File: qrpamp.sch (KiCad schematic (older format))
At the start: 0 parts

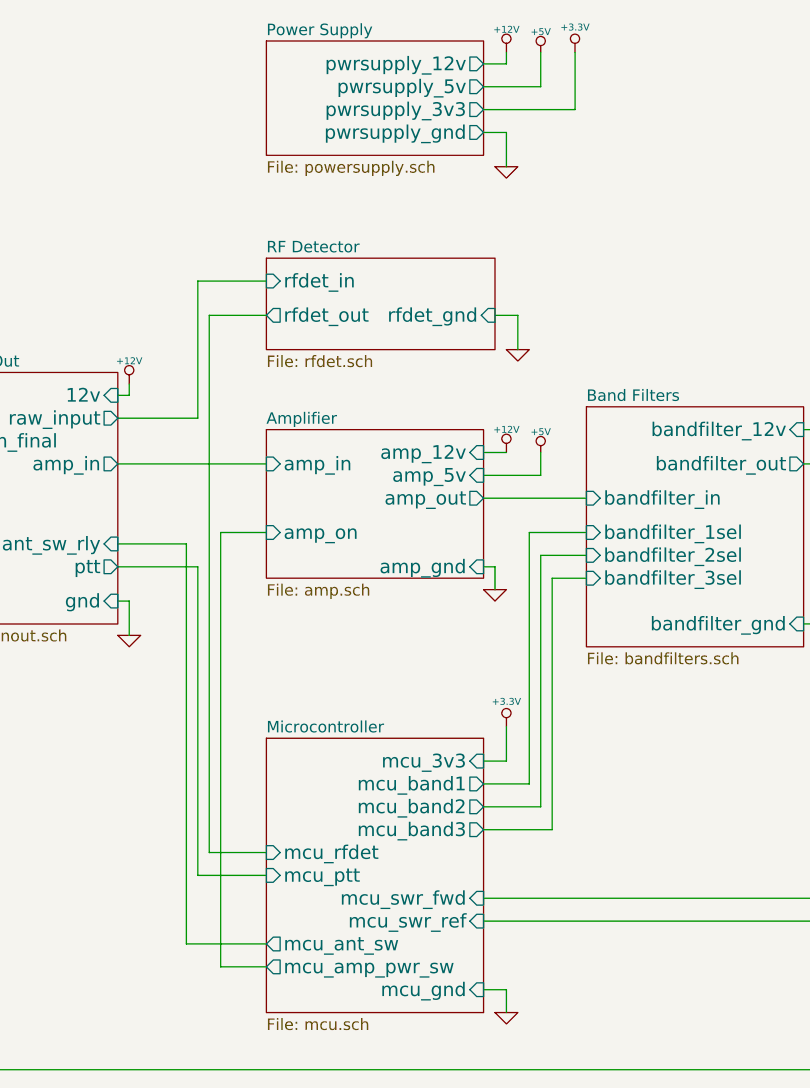
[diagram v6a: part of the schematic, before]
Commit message: Separate analog/digital gnd. Add some filtering caps and reset button.
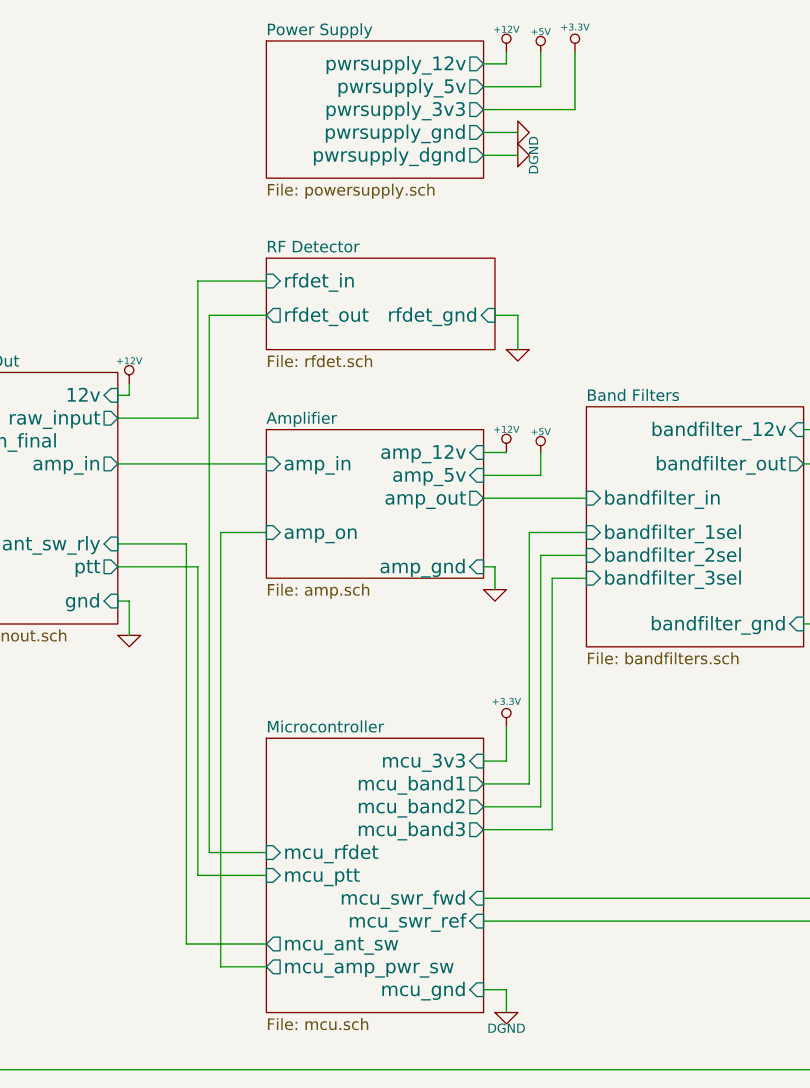
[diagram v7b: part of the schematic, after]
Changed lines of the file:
@@
 $EndSheet
 $Sheet
-S 3250 2000 950  500
+S 3250 2000 950  600
 U 5470C5E9
 F0 "Power Supply" 50
@@
 F4 "pwrsupply_3v3" O R 4200 2300 60
 F5 "pwrsupply_gnd" O R 4200 2400 60
+F6 "pwrsupply_dgnd" O R 4200 2500 60
 $EndSheet
 $Sheet
@@
 L GND #PWR01
 U 1 1 547173E7
-P 4300 2550
-F 0 "#PWR01" H 4300 2550 30  0001 C CNN
-F 1 "GND" H 4300 2480 30  0001 C CNN
-F 2 "" H 4300 2550 60  0000 C CNN
-F 3 "" H 4300 2550 60  0000 C CNN
-	1    4300 2550
-	1    0    0    -1
+P 4350 2400
+F 0 "#PWR01" H 4350 2400 30  0001 C CNN
+F 1 "GND" H 4350 2330 30  0001 C CNN
+F 2 "" H 4350 2400 60  0000 C CNN
+F 3 "" H 4350 2400 60  0000 C CNN
+	1    4350 2400
+	0    -1   -1   0
 $EndComp
 $Comp
@@
 Wire Wire Line
 	4600 2300 4200 2300
-Wire Wire Line
-	4200 2400 4300 2400
-Wire Wire Line
-	4300 2400 4300 2550
 $Comp
 L +12V #PWR05
@@
 Wire Wire Line
 	4300 5150 4300 5000
-$Comp
-L GND #PWR012
-U 1 1 5472B833
-P 4300 6250
-F 0 "#PWR012" H 4300 6250 30  0001 C CNN
-F 1 "GND" H 4300 6180 30  0001 C CNN
-F 2 "" H 4300 6250 60  0000 C CNN
-F 3 "" H 4300 6250 60  0000 C CNN
-	1    4300 6250
-	1    0    0    -1
-$EndComp
 Wire Wire Line
 	4200 6150 4300 6150
@@
 	3050 4150 3250 4150
 $Comp
-L +12V #PWR013
+L +12V #PWR012
 U 1 1 54742ADC
 P 2650 3500
-F 0 "#PWR013" H 2650 3450 20  0001 C CNN
+F 0 "#PWR012" H 2650 3450 20  0001 C CNN
 F 1 "+12V" H 2650 3600 30  0000 C CNN
 F 2 "" H 2650 3500 60  0000 C CNN
@@
 $EndComp
 $Comp
-L GND #PWR014
+L GND #PWR013
 U 1 1 54742BE9
 P 2650 4600
-F 0 "#PWR014" H 2650 4600 30  0001 C CNN
+F 0 "#PWR013" H 2650 4600 30  0001 C CNN
 F 1 "GND" H 2650 4530 30  0001 C CNN
 F 2 "" H 2650 4600 60  0000 C CNN
@@
 	2650 4450 2650 4600
 $Comp
-L GND #PWR015
+L GND #PWR014
 U 1 1 5474324F
 P 4350 3350
-F 0 "#PWR015" H 4350 3350 30  0001 C CNN
+F 0 "#PWR014" H 4350 3350 30  0001 C CNN
 F 1 "GND" H 4350 3280 30  0001 C CNN
 F 2 "" H 4350 3350 60  0000 C CNN
@@
 Wire Wire Line
 	4350 3200 4350 3350
+Wire Wire Line
+	4200 2400 4350 2400
+$Comp
+L DGND #PWR015
+U 1 1 548478BE
+P 4350 2500
+F 0 "#PWR015" H 4350 2500 40  0001 C CNN
+F 1 "DGND" H 4350 2430 40  0000 C CNN
+F 2 "" H 4350 2500 60  0000 C CNN
+F 3 "" H 4350 2500 60  0000 C CNN
+	1    4350 2500
+	0    -1   -1   0
+$EndComp
+Wire Wire Line
+	4200 2500 4350 2500
+$Comp
+L DGND #PWR016
+U 1 1 5484F0B9
+P 4300 6250
+F 0 "#PWR016" H 4300 6250 40  0001 C CNN
+F 1 "DGND" H 4300 6180 40  0000 C CNN
+F 2 "" H 4300 6250 60  0000 C CNN
+F 3 "" H 4300 6250 60  0000 C CNN
+	1    4300 6250
+	1    0    0    -1
+$EndComp
 $EndSCHEMATC

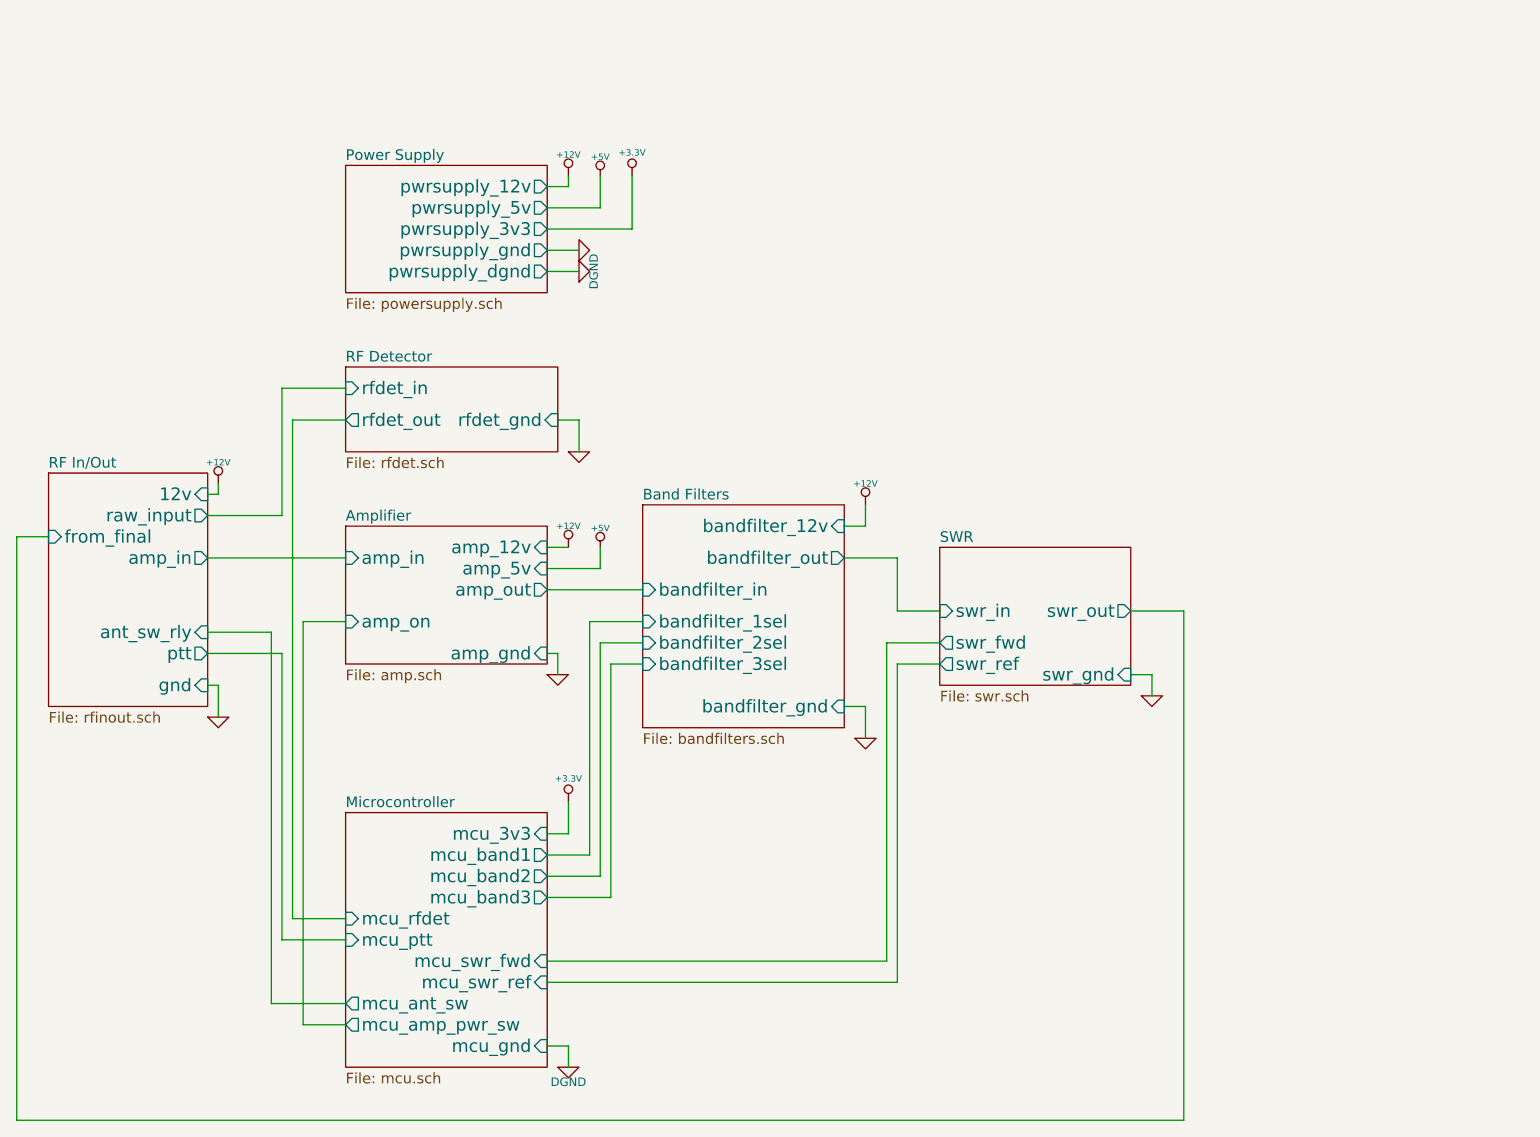
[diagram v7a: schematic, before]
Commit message: Fixed issues found with test board
- Added MOSFETs to relay switch lines from MCU
- Reconnected SWR in/out to actual ADC pins
- Changed LM3940 footprint to SOT223
- Added 4th mounting hole
- Swapped joystick for nav button
- Extended pads of STM32F401 for easier soldering
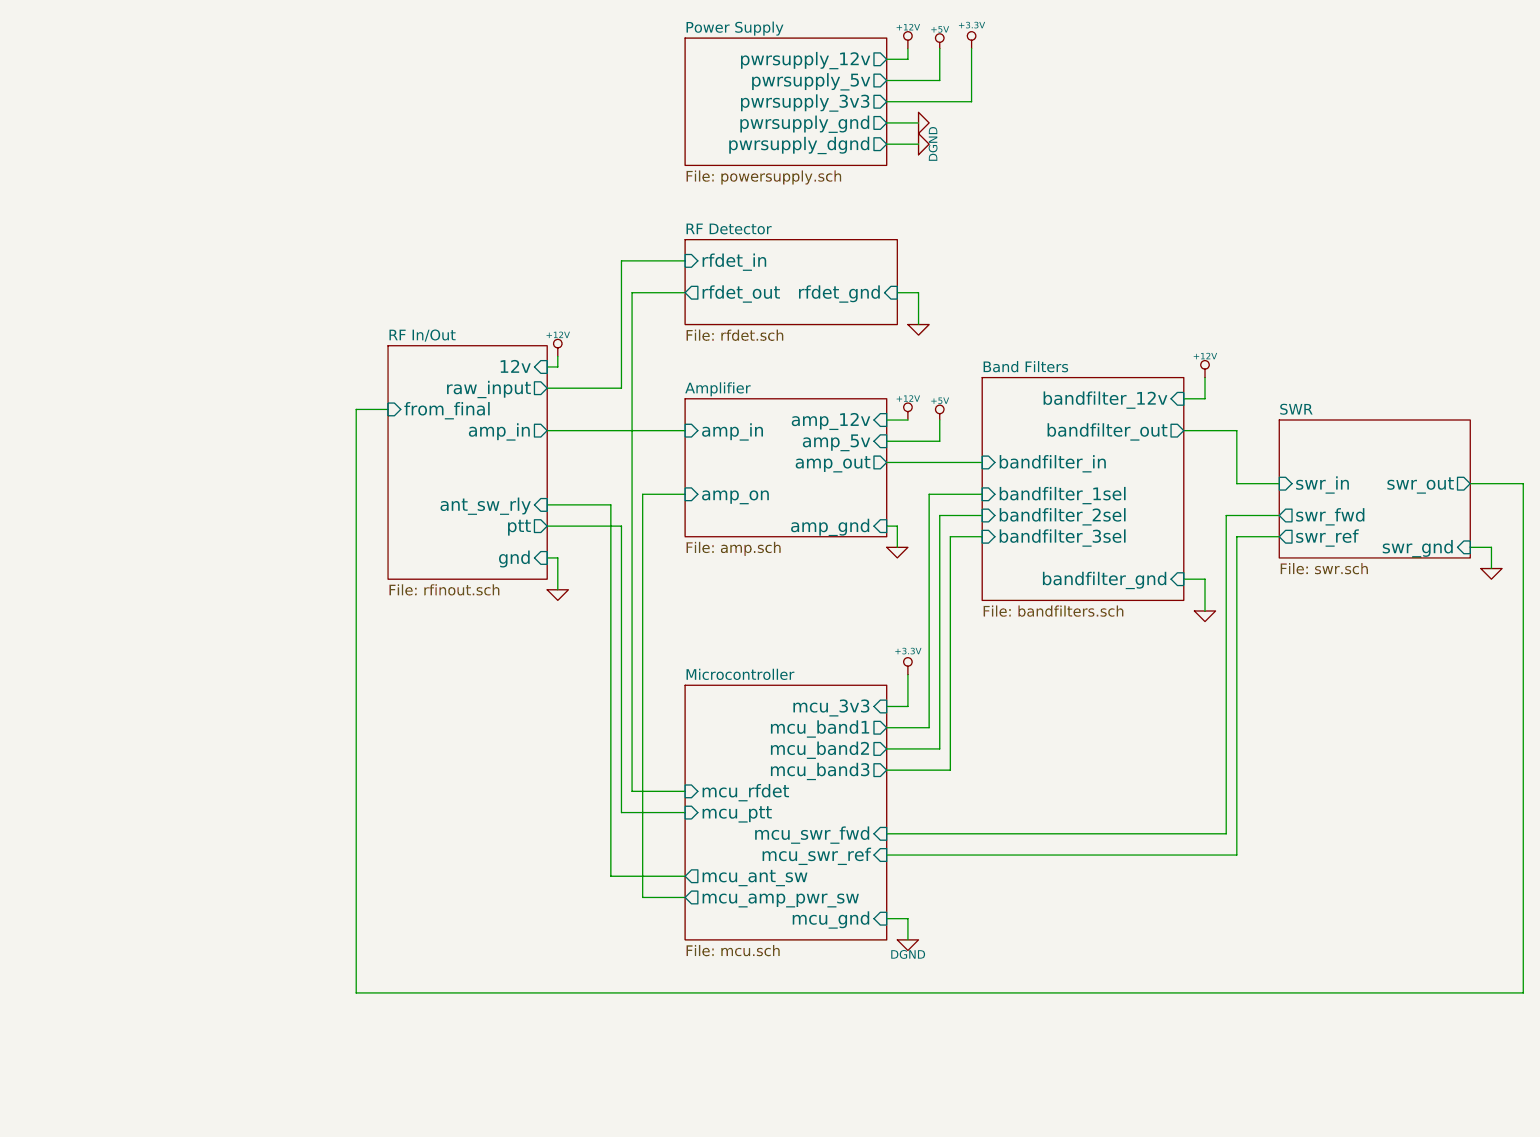
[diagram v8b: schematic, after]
